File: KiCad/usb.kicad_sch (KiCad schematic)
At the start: 15 parts, among them J20 RJE361882415, J22 USB3_A_Stacked, J23 USB3_IDC, J24 Conn_01x04, J25 Conn_01x05, U28 H5VU25U, U29 H5VU25U, U30 H5VU25U, U31 H5VU25U, U32 H5VU25U, U33 H5VU25U, U34 H5VU25U, U35 H5VU25U, U36 H5VU25U, U37 H5VU25U

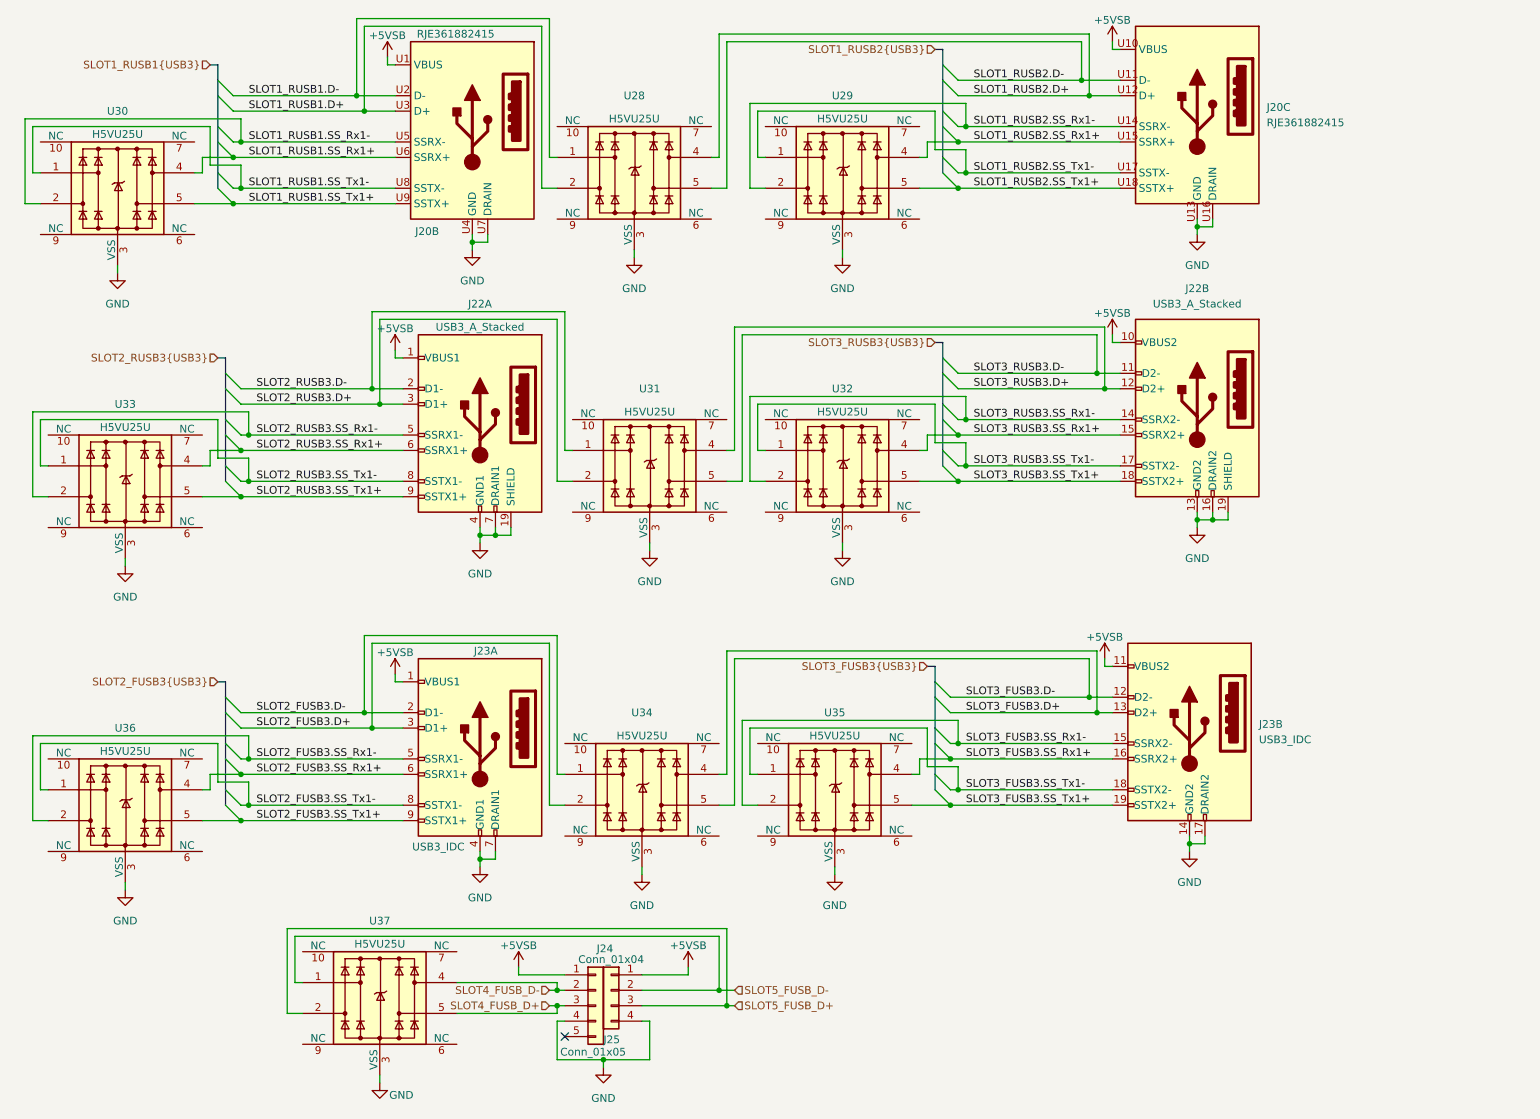
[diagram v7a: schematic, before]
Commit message: Fix more footprint issues, continue laying out components
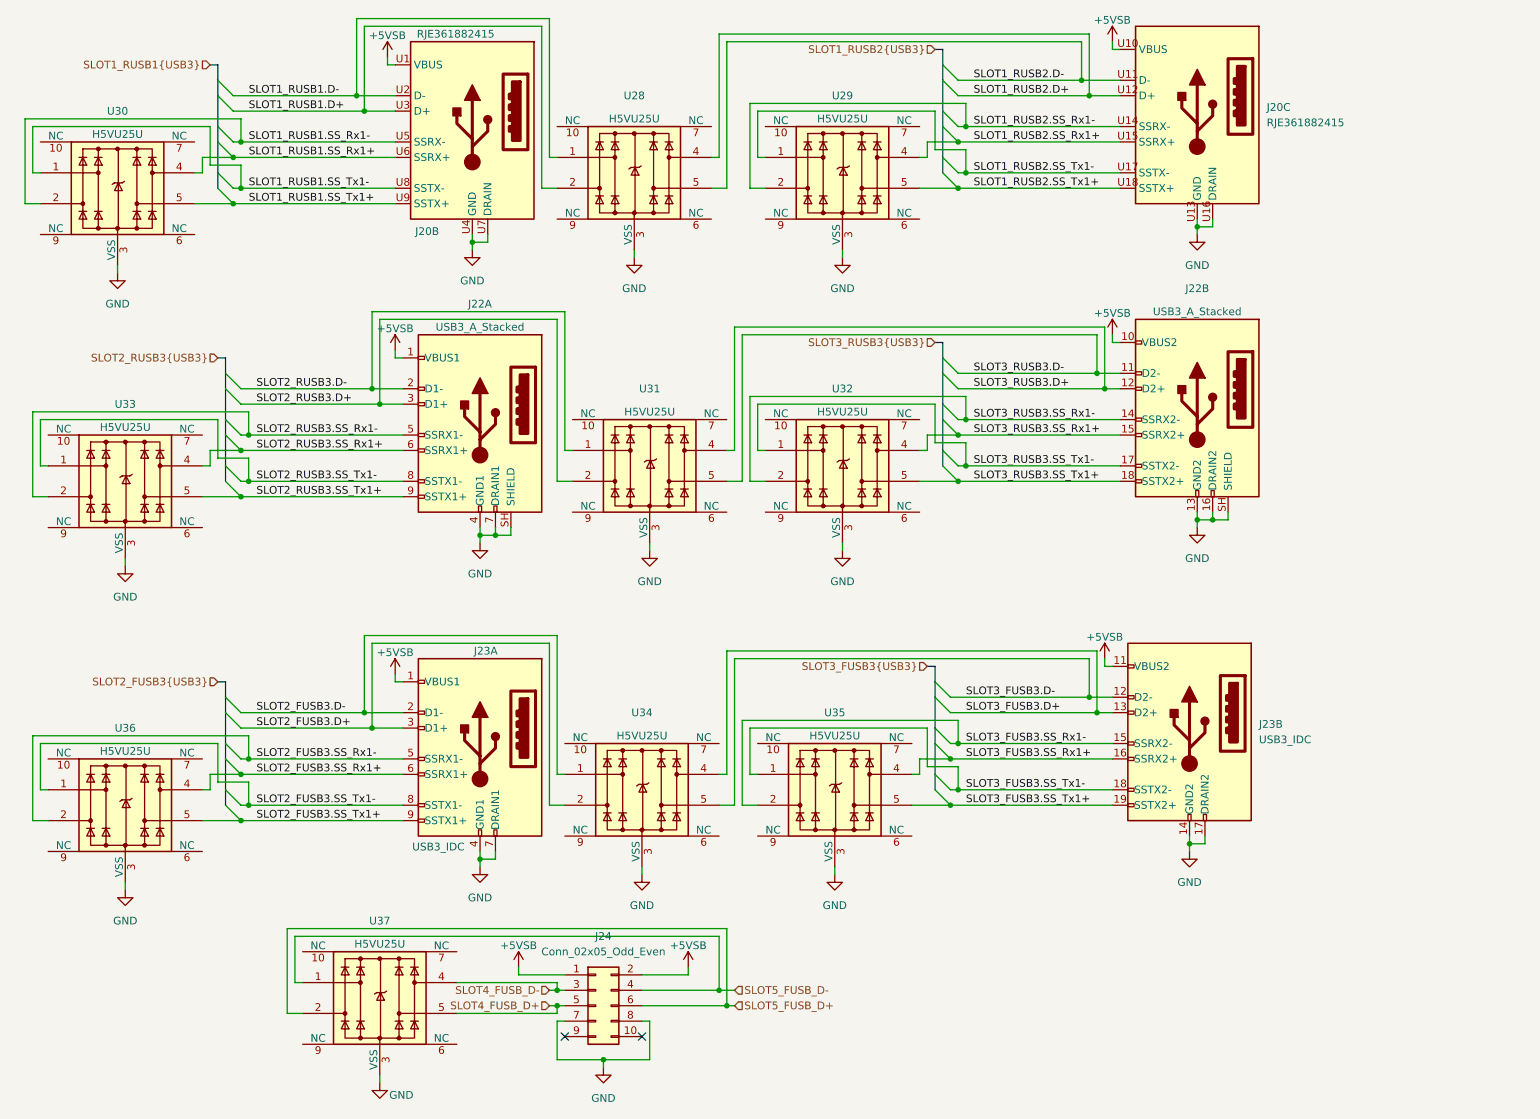
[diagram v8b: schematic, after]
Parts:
- removed J24: Conn_01x04, Connector_PinHeader_2.54mm:PinHeader_1x04_P2.54mm_Vertical, symbol Connector_Generic:Conn_01x04
- removed J25: Conn_01x05, Connector_PinHeader_2.54mm:PinHeader_1x05_P2.54mm_Vertical, symbol Connector_Generic:Conn_01x05
- added J24: Conn_02x05_Odd_Even, Connector_PinHeader_2.54mm:PinHeader_2x05_P2.54mm_Vertical, symbol Connector_Generic:Conn_02x05_Odd_Even
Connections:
- net +5VSB: now also J24.1 (Pin_1), J24.2 (Pin_2)
- net GND: now also J22.SH (SHIELD), J22.SH (SHIELD), J24.7 (Pin_7), J24.8 (Pin_8); no longer J22.19 (SHIELD), J22.19 (SHIELD)
- net SLOT4_FUSB_D+: now also J24.5 (Pin_5)
- net SLOT4_FUSB_D-: now also J24.3 (Pin_3)
- net SLOT5_FUSB_D+: now also J24.6 (Pin_6)
- net SLOT5_FUSB_D-: now also J24.4 (Pin_4)
- no-connect marks 1 -> 2
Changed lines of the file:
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@@
 		(at 104.14 185.42)
 	)
+	(no_connect
+		(at 116.84 185.42)
+	)
 	(bus_entry
 		(at 165.1 134.62)
@@
 	)
 	(symbol
+		(lib_id "Connector_Generic:Conn_02x05_Odd_Even")
+		(at 109.22 180.34 0)
+		(unit 1)
+		(exclude_from_sim no)
+		(in_bom yes)
+		(on_board yes)
+		(dnp no)
+		(fields_autoplaced yes)
+		(property "Reference" "J24"
+			(at 110.49 168.91 0)
+			(effects
+				(font
+					(size 1.27 1.27)
+				)
+			)
+		)
+		(property "Value" "Conn_02x05_Odd_Even"
+			(at 110.49 171.45 0)
+			(effects
+				(font
+					(size 1.27 1.27)
+				)
+			)
+		)
+		(property "Footprint" "Connector_PinHeader_2.54mm:PinHeader_2x05_P2.54mm_Vertical"
+			(at 109.22 180.34 0)
+			(effects
+				(font
+					(size 1.27 1.27)
+				)
+				(hide yes)
+			)
+		)
+		(property "Datasheet" "~"
+			(at 109.22 180.34 0)
+			(effects
+				(font
+					(size 1.27 1.27)
+				)
+				(hide yes)
+			)
+		)
+		(property "Description" "Generic connector, double row, 02x05, odd/even pin numbering scheme (row 1 odd numbers, row 2 even numbers), script generated (kicad-library-utils/schlib/autogen/connector/)"
+			(at 109.22 180.34 0)
+			(effects
+				(font
+					(size 1.27 1.27)
+				)
+				(hide yes)
+			)
+		)
+		(pin "3"
+		)
+		(pin "2"
+		)
+		(pin "4"
+		)
+		(pin "9"
+		)
+		(pin "5"
+		)
+		(pin "7"
+		)
+		(pin "10"
+		)
+		(pin "8"
+		)
+		(pin "1"
+		)
+		(pin "6"
+		)
+		(instances
+			(project ""
+				(path "/49abeb3a-c598-45a3-ba6b-595eb04f17a8/aeaf6077-b212-49fa-a33e-8ac7d8738247"
+					(reference "J24")
+					(unit 1)
+				)
+			)
+		)
+	)
+	(symbol
 		(lib_id "power:GND")
 		(at 118.11 105.41 0)
@@
 	)
 	(symbol
-		(lib_id "Connector_Generic:Conn_01x05")
-		(at 109.22 180.34 0)
-		(unit 1)
-		(exclude_from_sim no)
-		(in_bom yes)
-		(on_board yes)
-		(dnp no)
-		(property "Reference" "J25"
-			(at 110.49 185.928 0)
-			(effects
-				(font
-					(size 1.27 1.27)
-				)
-				(justify left)
-			)
-		)
-		(property "Value" "Conn_01x05"
-			(at 103.378 187.96 0)
-			(effects
-				(font
-					(size 1.27 1.27)
-				)
-				(justify left)
-			)
-		)
-		(property "Footprint" "Connector_PinHeader_2.54mm:PinHeader_1x05_P2.54mm_Vertical"
-			(at 109.22 180.34 0)
-			(effects
-				(font
-					(size 1.27 1.27)
-				)
-				(hide yes)
-			)
-		)
-		(property "Datasheet" "~"
-			(at 109.22 180.34 0)
-			(effects
-				(font
-					(size 1.27 1.27)
-				)
-				(hide yes)
-			)
-		)
-		(property "Description" "Generic connector, single row, 01x05, script generated (kicad-library-utils/schlib/autogen/connector/)"
-			(at 109.22 180.34 0)
-			(effects
-				(font
-					(size 1.27 1.27)
-				)
-				(hide yes)
-			)
-		)
-		(pin "3"
-		)
-		(pin "4"
-		)
-		(pin "2"
-		)
-		(pin "1"
-		)
-		(pin "5"
-		)
-		(instances
-			(project ""
-				(path "/49abeb3a-c598-45a3-ba6b-595eb04f17a8/aeaf6077-b212-49fa-a33e-8ac7d8738247"
-					(reference "J25")
-					(unit 1)
-				)
-			)
-		)
-	)
-	(symbol
 		(lib_id "power:+5V")
 		(at 124.46 173.99 0)
@@
 	)
 	(symbol
+		(lib_name "USB3_A_Stacked_1")
 		(lib_id "Connector:USB3_A_Stacked")
 		(at 208.28 81.28 0)
@@
 		)
 		(property "Value" "USB3_A_Stacked"
-			(at 208.28 64.77 0)
+			(at 208.28 66.04 0)
 			(effects
 				(font
@@
 		(pin "7"
 		)
-		(pin "19"
+		(pin "SH"
 		)
 		(pin "8"
@@
 	)
 	(symbol
-		(lib_id "Connector_Generic:Conn_01x04")
-		(at 111.76 177.8 0)
-		(mirror y)
-		(unit 1)
-		(exclude_from_sim no)
-		(in_bom yes)
-		(on_board yes)
-		(dnp no)
-		(property "Reference" "J24"
-			(at 110.744 170.942 0)
-			(effects
-				(font
-					(size 1.27 1.27)
-				)
-			)
-		)
-		(property "Value" "Conn_01x04"
-			(at 111.76 172.72 0)
-			(effects
-				(font
-					(size 1.27 1.27)
-				)
-			)
-		)
-		(property "Footprint" "Connector_PinHeader_2.54mm:PinHeader_1x04_P2.54mm_Vertical"
-			(at 111.76 177.8 0)
-			(effects
-				(font
-					(size 1.27 1.27)
-				)
-				(hide yes)
-			)
-		)
-		(property "Datasheet" "~"
-			(at 111.76 177.8 0)
-			(effects
-				(font
-					(size 1.27 1.27)
-				)
-				(hide yes)
-			)
-		)
-		(property "Description" "Generic connector, single row, 01x04, script generated (kicad-library-utils/schlib/autogen/connector/)"
-			(at 111.76 177.8 0)
-			(effects
-				(font
-					(size 1.27 1.27)
-				)
-				(hide yes)
-			)
-		)
-		(pin "1"
-		)
-		(pin "2"
-		)
-		(pin "4"
-		)
-		(pin "3"
-		)
-		(instances
-			(project ""
-				(path "/49abeb3a-c598-45a3-ba6b-595eb04f17a8/aeaf6077-b212-49fa-a33e-8ac7d8738247"
-					(reference "J24")
-					(unit 1)
-				)
-			)
-		)
-	)
-	(symbol
 		(lib_id "power:GND")
 		(at 208.28 53.34 0)
@@
 		(pin "7"
 		)
-		(pin "19"
+		(pin "SH"
 		)
 		(pin "8"
